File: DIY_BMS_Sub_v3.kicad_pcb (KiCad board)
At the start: 2 copper layers, 80 x 100 mm, 75 parts, among them J1 Conn_02x10_Top_Bottom, J2 Conn_02x05_Top_Bottom, Q1 BUK9M20-40HX, Q2 BUK9M20-40HX, Q3 BUK9M20-40HX, Q4 BUK9M20-40HX, Q5 BUK9M20-40HX, Q6 BUK9M20-40HX, U1 BQ76PL536A

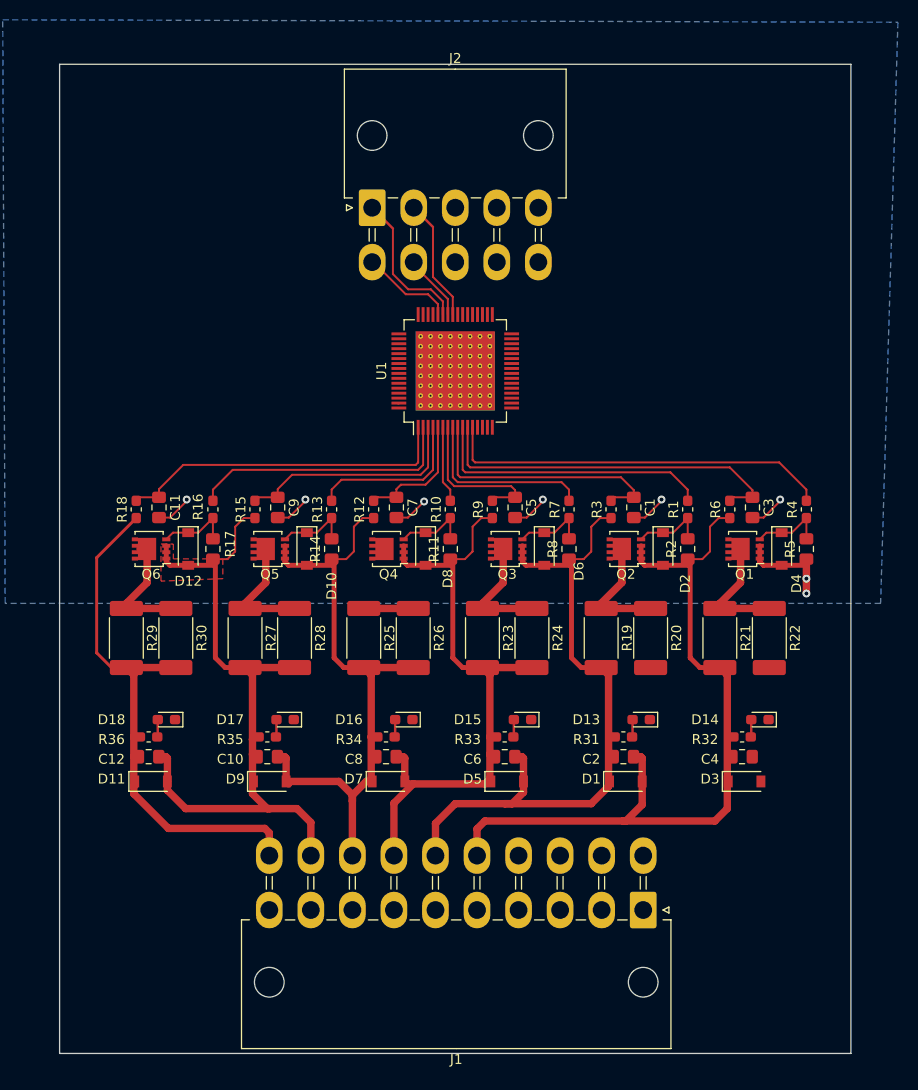
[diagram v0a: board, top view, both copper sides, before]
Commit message: Add files via upload
(re)labeled SPI-host pins to 10-pin connector. Added DIP-switch to South. Started placing decoupling capacitors.
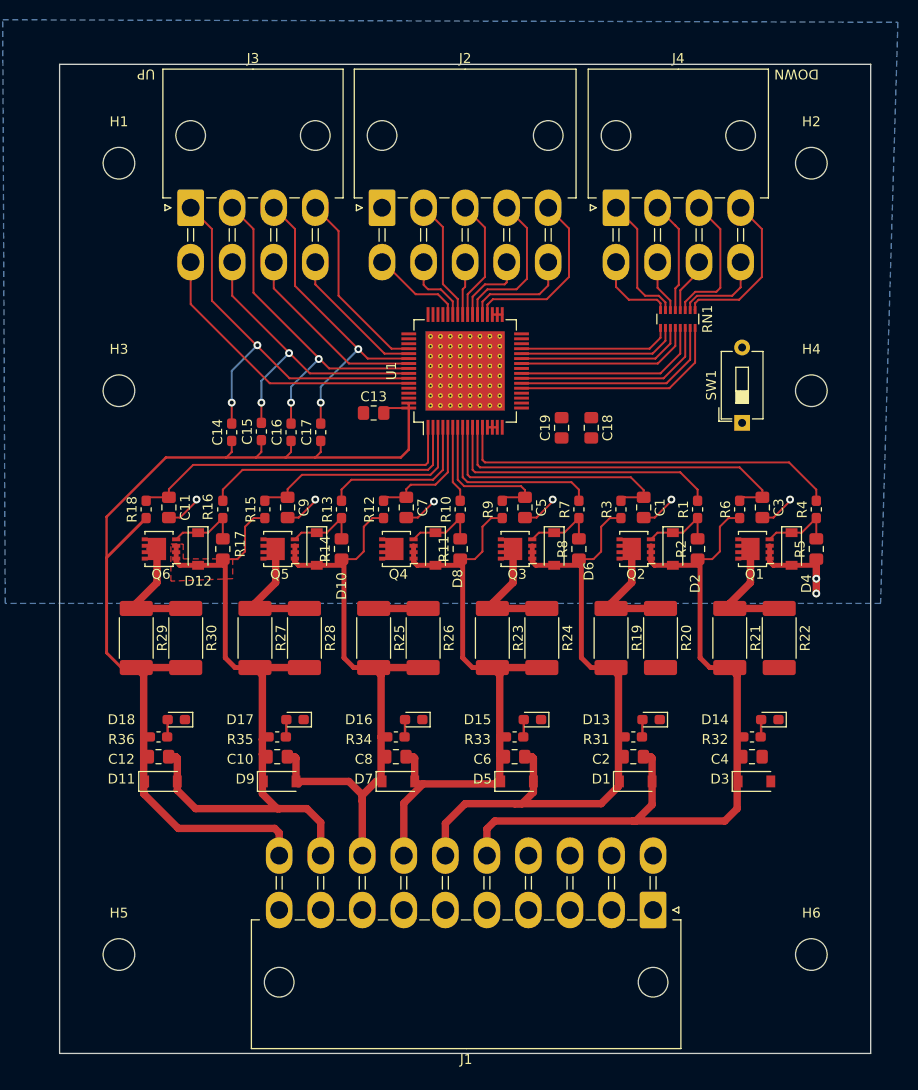
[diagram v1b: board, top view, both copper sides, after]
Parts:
- added C13: 0.1u, Capacitor_SMD:C_0805_2012Metric_Pad1.15x1.40mm_HandSolder, F.Cu at (31.8, 35.2)
- added C14: 33p, Capacitor_SMD:C_0603_1608Metric_Pad1.05x0.95mm_HandSolder, F.Cu at (17.4, 37.2)
- added C15: 33p, Capacitor_SMD:C_0603_1608Metric_Pad1.05x0.95mm_HandSolder, F.Cu at (20.4, 37.1)
- added C16: 33p, Capacitor_SMD:C_0603_1608Metric_Pad1.05x0.95mm_HandSolder, F.Cu at (23.4, 37.2)
- added C17: 33p, Capacitor_SMD:C_0603_1608Metric_Pad1.05x0.95mm_HandSolder, F.Cu at (26.4, 37.2)
- added C18: 0.1u, Capacitor_SMD:C_0805_2012Metric_Pad1.15x1.40mm_HandSolder, F.Cu at (53.8, 36.8)
- added C19: 0.1u, Capacitor_SMD:C_0805_2012Metric_Pad1.15x1.40mm_HandSolder, F.Cu at (50.8, 36.8)
- added H1: MountingHole, MountingHole:MountingHole_3.2mm_M3, F.Cu at (6.00, 10.0)
- added H2: MountingHole, MountingHole:MountingHole_3.2mm_M3, F.Cu at (76.0, 10.0)
- added H3: MountingHole, MountingHole:MountingHole_3.2mm_M3, F.Cu at (6.00, 33.0)
- added H4: MountingHole, MountingHole:MountingHole_3.2mm_M3, F.Cu at (76.0, 33.0)
- added H5: MountingHole, MountingHole:MountingHole_3.2mm_M3, F.Cu at (6.00, 90.0)
- added H6: MountingHole, MountingHole:MountingHole_3.2mm_M3, F.Cu at (76.0, 90.0)
- added J3: Conn_02x04_Top_Bottom, Connector_Molex:Molex_Mini-Fit_Jr_5569-08A2_2x04_P4.20mm_Horizontal, F.Cu at (13.2, 14.5)
- added J4: Conn_02x04_Top_Bottom, Connector_Molex:Molex_Mini-Fit_Jr_5569-08A2_2x04_P4.20mm_Horizontal, F.Cu at (56.2, 14.5)
- added RN1: 1K_Pack08, Resistor_SMD:R_Array_Convex_8x0602, F.Cu at (62.5, 25.8)
- added SW1: SW_DIP_x01, Button_Switch_THT:SW_DIP_SPSTx01_Slide_6.7x4.1mm_W7.62mm_P2.54mm_LowProfile, F.Cu at (69.0, 36.2)
- moved C1 1.00 mm to (59.0, 44.8)
- moved C10 1.00 mm to (22.0, 70.0)
- moved C11 1.00 mm to (11.1, 44.8)
- moved C12 1.00 mm to (10.0, 70.0)
- moved C2 1.00 mm to (58.0, 70.0)
- moved C3 1.00 mm to (71.0, 44.8)
- moved C4 1.00 mm to (70.0, 70.0)
- moved C5 1.00 mm to (47.0, 44.8)
- moved C6 1.00 mm to (46.0, 70.0)
- moved C7 1.00 mm to (35.0, 44.8)
- moved C8 1.00 mm to (34.0, 70.0)
- moved C9 1.00 mm to (23.1, 44.8)
- moved D1 1.00 mm to (58.2, 72.5)
- moved D10 1.00 mm to (26.0, 49.0)
- moved D11 1.00 mm to (10.2, 72.5)
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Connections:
- J2 pad 1: CS_H -> AGND
- J2 pad 10: (no net) -> DRDY_H
- J2 pad 2: SDO_H -> SDI_H
- J2 pad 3: (no net) -> SCLK_H
- J2 pad 4: (no net) -> ALERT_H
- J2 pad 5: (no net) -> CONV_H
- J2 pad 7: SDI_H -> CS_H
- J2 pad 8: (no net) -> SDO_H
- J2 pad 9: (no net) -> FAULT_H
- U1 pad 14: (no net) -> AGND
- U1 pad 15: (no net) -> AGND
- U1 pad 17: (no net) -> Net-(C19-Pad2)
- U1 pad 18: (no net) -> Net-(C18-Pad1)
- U1 pad 21: (no net) -> Net-(RN1-Pad16)
- U1 pad 22: (no net) -> Net-(RN1-Pad15)
- U1 pad 23: (no net) -> Net-(RN1-Pad14)
- U1 pad 24: (no net) -> Net-(RN1-Pad13)
- U1 pad 25: (no net) -> AGND
- U1 pad 26: (no net) -> Net-(RN1-Pad12)
- U1 pad 27: (no net) -> Net-(RN1-Pad11)
- U1 pad 28: (no net) -> Net-(RN1-Pad10)
- U1 pad 29: (no net) -> Net-(RN1-Pad9)
- U1 pad 33: (no net) -> AGND
- U1 pad 34: (no net) -> AGND
- U1 pad 35: (no net) -> AGND
- U1 pad 36: (no net) -> CONV_H
- U1 pad 37: (no net) -> DRDY_H
- U1 pad 38: (no net) -> ALERT_H
- U1 pad 39: (no net) -> FAULT_H
- U1 pad 40: (no net) -> SCLK_H
- U1 pad 46: (no net) -> Net-(C18-Pad1)
- U1 pad 49: (no net) -> AGND
- U1 pad 50: (no net) -> AGND
- U1 pad 52: (no net) -> CS_N
- U1 pad 53: (no net) -> SDI_N
- U1 pad 54: (no net) -> SDO_N
- U1 pad 55: (no net) -> SCLK_N
- U1 pad 56: (no net) -> FAULT_N
- U1 pad 57: (no net) -> ALERT_N
- U1 pad 58: (no net) -> DRDY_N
- U1 pad 59: (no net) -> CONV_N
- U1 pad 63: (no net) -> S6
- U1 pad 64: (no net) -> S6
- U1 pad 65: Net-(U1-Pad65) -> AGND
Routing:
- net S6: track 56.2 -> 108.9 mm
- net DRDY_N: track 0.00 -> 42.4 mm, vias 0 -> 2
- net FAULT_N: track 0.00 -> 36.0 mm, vias 0 -> 2
- net ALERT_N: track 0.00 -> 32.7 mm, vias 0 -> 2
- net SDO_N: track 0.00 -> 32.4 mm, vias 0 -> 2
- net CONV_N: track 0.00 -> 29.6 mm
- net Net-(RN1-Pad16): track 0.00 -> 22.1 mm
- net Net-(RN1-Pad15): track 0.00 -> 21.2 mm
- net Net-(RN1-Pad14): track 0.00 -> 20.4 mm
- net Net-(RN1-Pad13): track 0.00 -> 19.5 mm
- net SCLK_N: track 0.00 -> 19.4 mm
- net CS_N: track 0.00 -> 19.2 mm
- net CONV_H: track 0.00 -> 18.3 mm
- net Net-(RN1-Pad12): track 0.00 -> 18.1 mm
- net Net-(RN1-Pad11): track 0.00 -> 17.3 mm
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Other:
- board size 80 x 100 mm -> 82 x 100 mm
- board text added: "DOWN"
- board text added: "UP"

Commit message: Add files via upload
Finished adding decoupling caps. Added temperature sensor (TS1).
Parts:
- added C20: 2.2u, Capacitor_SMD:C_0805_2012Metric_Pad1.15x1.40mm_HandSolder, F.Cu at (59.8, 36.5)
- added C21: 2.2u, Capacitor_SMD:C_0805_2012Metric_Pad1.15x1.40mm_HandSolder, F.Cu at (54.0, 36.5)
- added C22: 10u, Capacitor_SMD:C_0805_2012Metric_Pad1.15x1.40mm_HandSolder, F.Cu at (47.8, 38.8)
- added C23: 2.2u, Capacitor_SMD:C_0805_2012Metric_Pad1.15x1.40mm_HandSolder, F.Cu at (50.5, 26.0)
- added C24: 47p, Capacitor_SMD:C_0805_2012Metric_Pad1.15x1.40mm_HandSolder, F.Cu at (70.8, 79.8)
- added R37: 1K47, Resistor_SMD:R_0603_1608Metric_Pad1.05x0.95mm_HandSolder, F.Cu at (66.8, 84.5)
- added R38: 1K82, Resistor_SMD:R_0603_1608Metric_Pad1.05x0.95mm_HandSolder, F.Cu at (71.2, 84.5)
- moved C18 3.76 mm to (57.5, 36.5)
- moved C19 1.03 mm to (51.8, 36.5)
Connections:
- J1 pad 11: (no net) -> 5VDC
- J1 pad 12: (no net) -> Temp-
- U1 pad 16: (no net) -> Net-(C22-Pad2)
- U1 pad 19: (no net) -> Net-(R38-Pad1)
- U1 pad 20: (no net) -> Net-(C24-Pad1)
- U1 pad 32: (no net) -> 5VDC

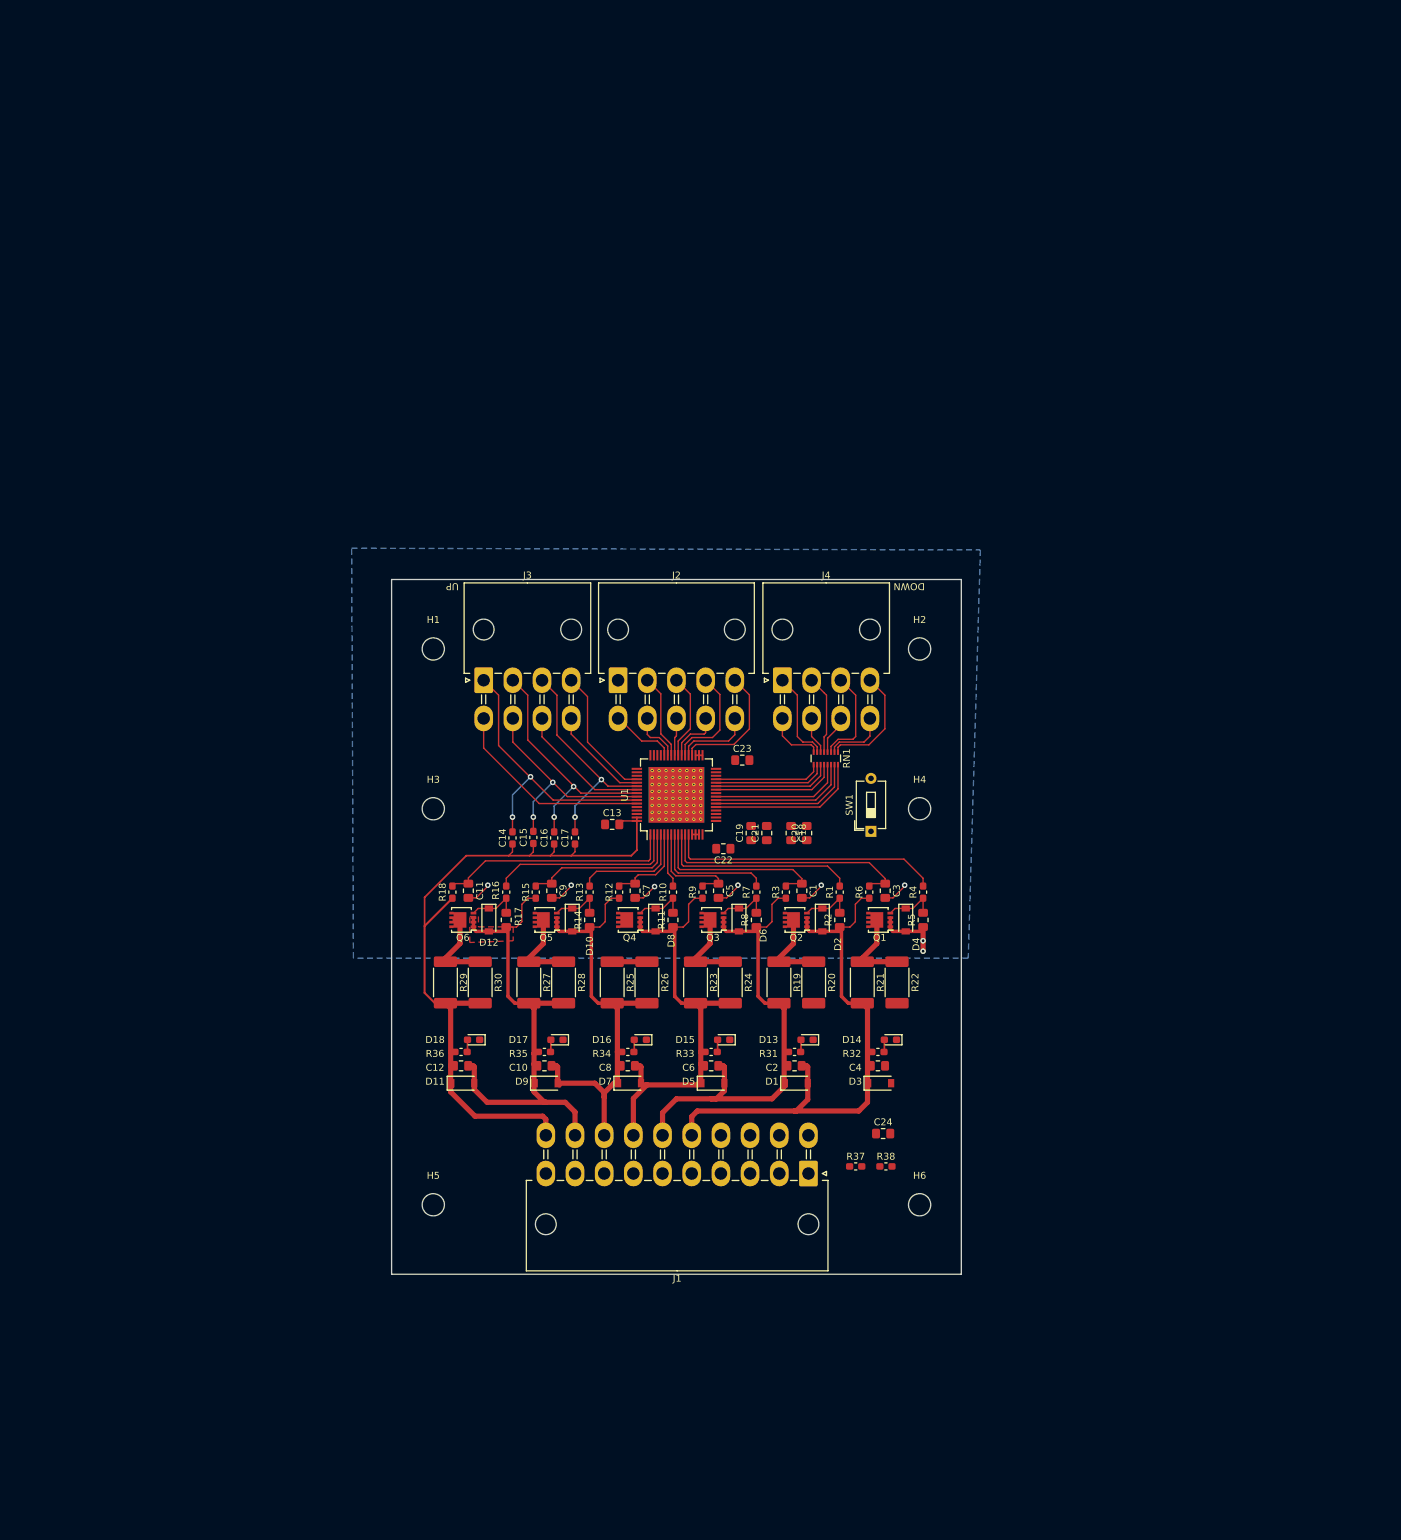
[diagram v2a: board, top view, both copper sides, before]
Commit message: Add files via upload
Added S1 and S2 traces in IN2-layer. Added stitching vias for outside groundplanes.
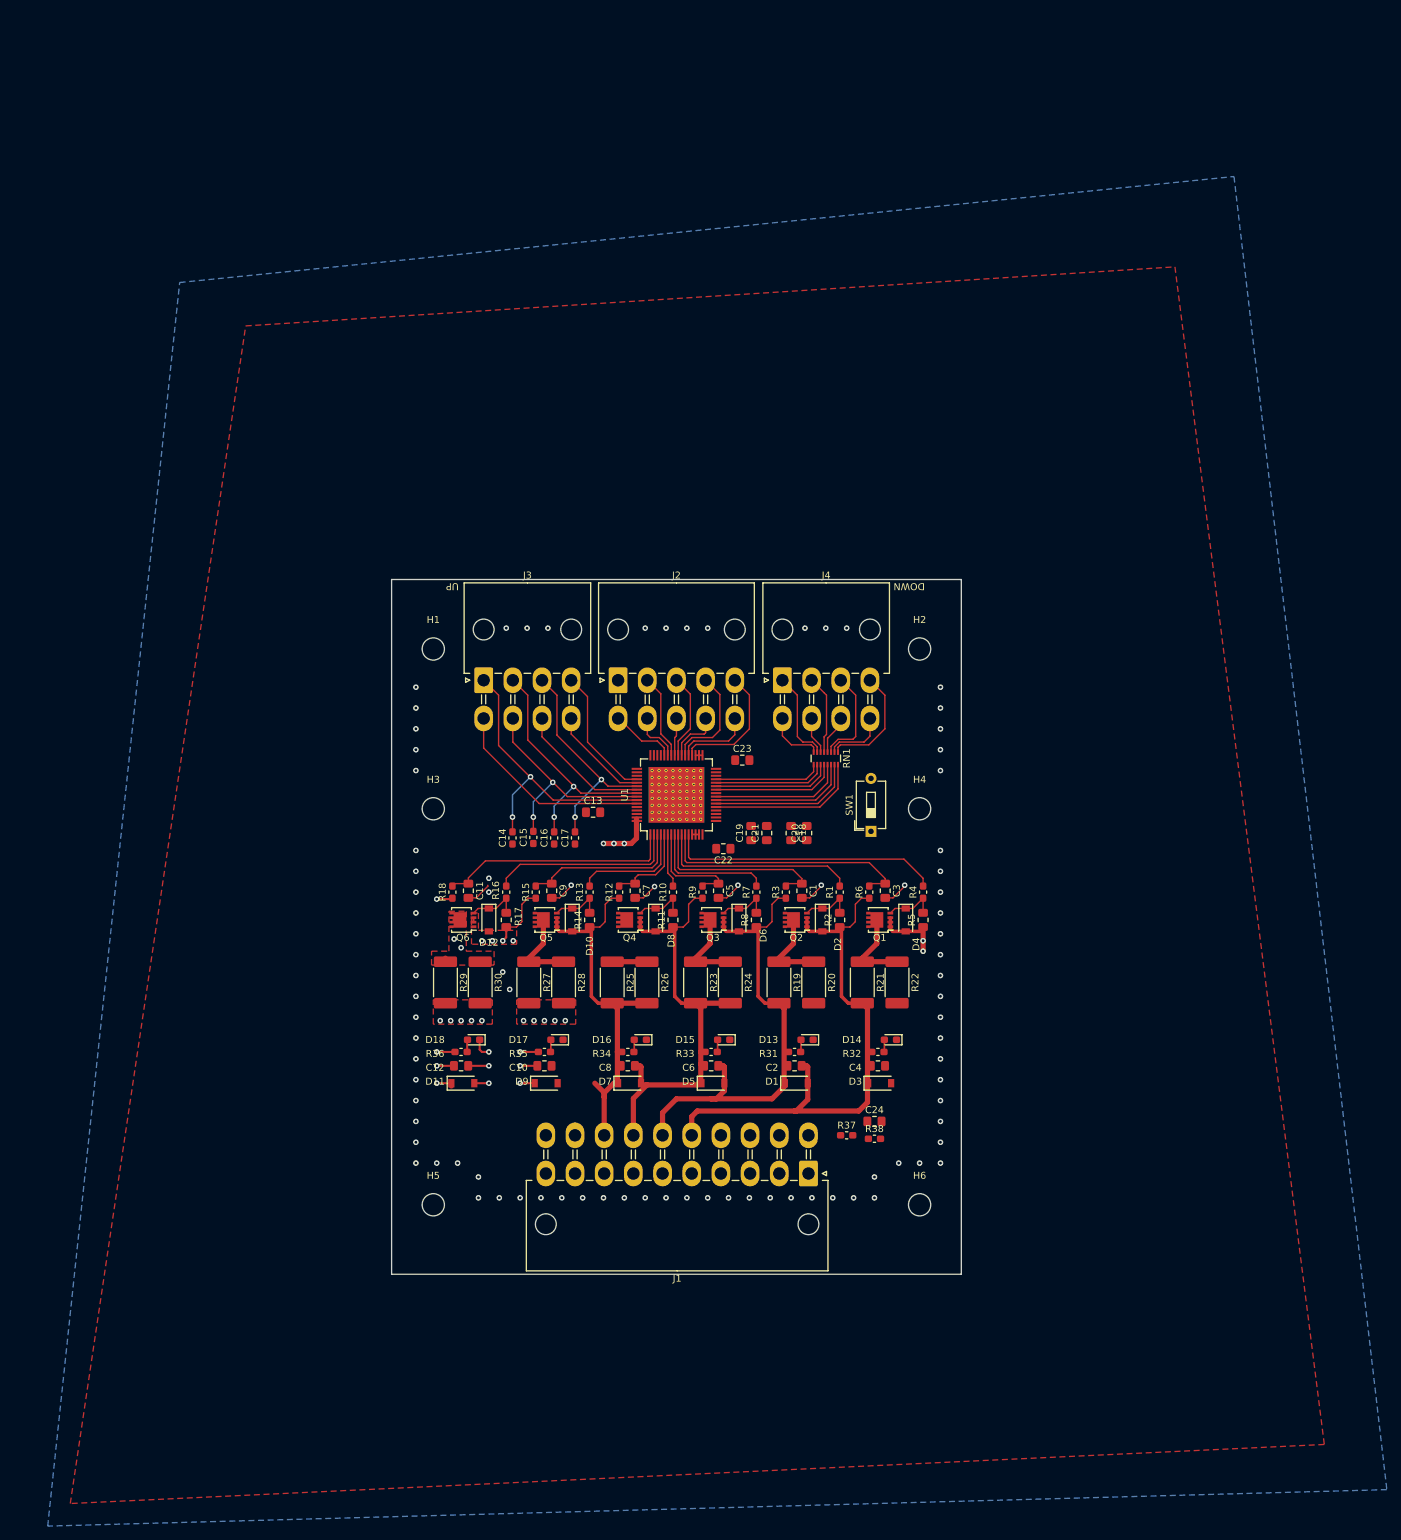
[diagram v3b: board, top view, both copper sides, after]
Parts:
- moved R37 4.66 mm to (65.5, 80.0)
- moved R38 4.31 mm to (69.5, 80.5)
- moved C13 3.26 mm to (29.0, 33.5)
- moved C24 2.15 mm to (69.5, 78.0)
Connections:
- J1 pad 4: (no net) -> AGND
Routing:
- net Net-(D18-Pad1): track 12.7 -> 25.5 mm, vias 0 -> 3
- net S4: track 66.8 -> 57.8 mm
- net S5: track 75.0 -> 78.6 mm, vias 0 -> 14
- net S6: track 108.9 -> 105.5 mm, vias 0 -> 12
- net AGND: vias 8 -> 89
- added copper zone on F.Cu, net Net-(D18-Pad1)
- added copper zone on F.Cu, net S5
- added copper zone on F.Cu, net S6
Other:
- copper layers 2 -> 4

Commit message: Add files via upload
Added 3d models for connectors (Molex). Started changing cell connections from Top-layer to IN1-layer.
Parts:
- J1: footprint Connector_Molex:Molex_Mini-Fit_Jr_5569-20A2_2x10_P4.20mm_Horizontal -> #_Connectors:Molex_Mini-Fit_Jr_5569-20A2_2x10_P4.20mm_Horizontal_with3d
- J2: footprint Connector_Molex:Molex_Mini-Fit_Jr_5569-10A2_2x05_P4.20mm_Horizontal -> #_Connectors:Molex_Mini-Fit_Jr_5569-10A2_2x05_P4.20mm_Horizontal_with3d
- J3, J4: footprint Connector_Molex:Molex_Mini-Fit_Jr_5569-08A2_2x04_P4.20mm_Horizontal -> #_Connectors:Molex_Mini-Fit_Jr_5569-08A2_2x04_P4.20mm_Horizontal_with3D
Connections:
- J1 pad 4: AGND -> (no net)
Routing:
- net S5: track 78.6 -> 43.0 mm, vias 14 -> 6
- net S6: track 105.5 -> 135.5 mm, vias 12 -> 17
- net S3: track 66.1 -> 79.4 mm
- net S1: track 79.4 -> 71.7 mm, vias 0 -> 3
- net Net-(D16-Pad1): track 5.00 -> 11.9 mm
- net S4: track 57.8 -> 56.9 mm, vias 0 -> 4
- net S2: track 69.4 -> 70.0 mm, vias 0 -> 3
- added copper zone on F.Cu, net S4
